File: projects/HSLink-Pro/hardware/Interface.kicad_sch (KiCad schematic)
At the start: 19 parts, among them J1 IDC 2x10p 夹板, J2 USB_C_Receptacle_USB2.0, Q1 AO3401A, Q2 2N7002, Q3 AO3401A, Q4 2N7002, U14 MT9700, U15 ESD0524P, U16 ESD0524P, U17 ESD0524P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

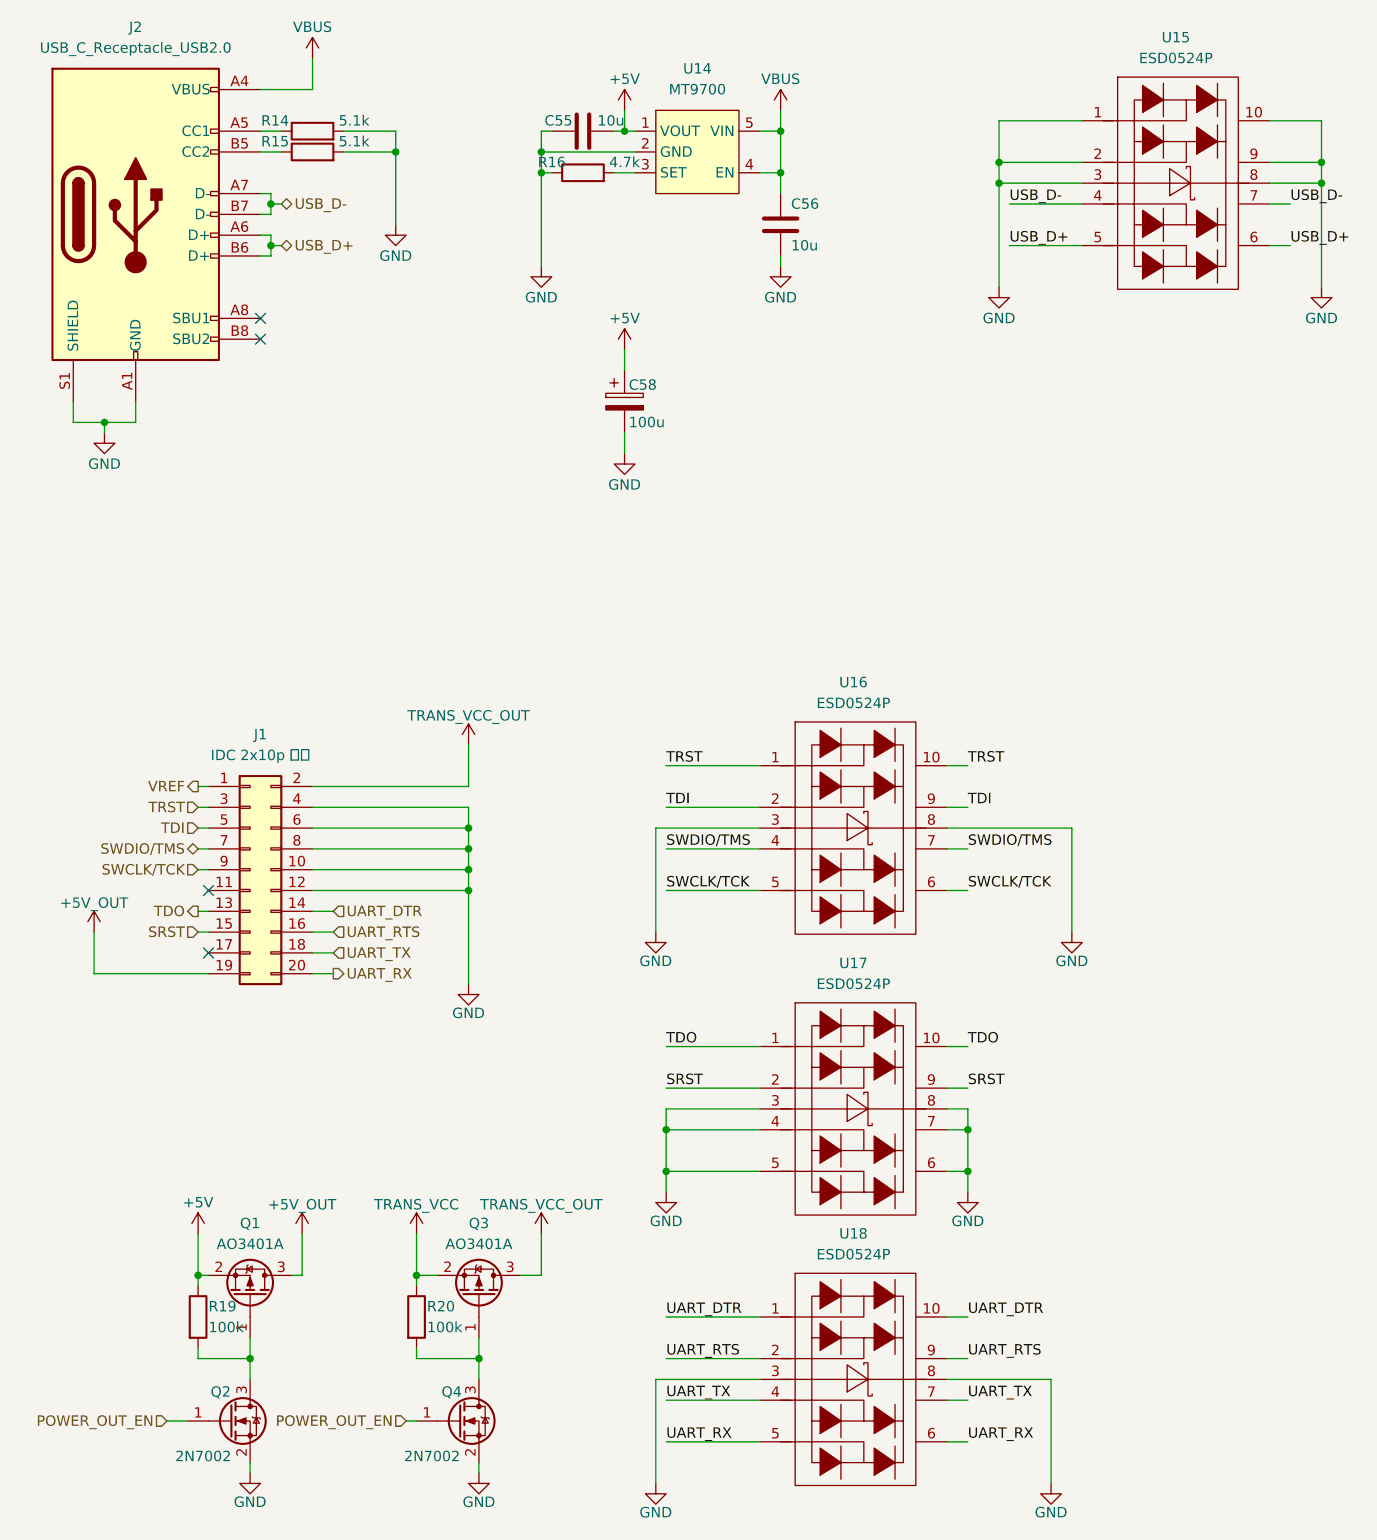
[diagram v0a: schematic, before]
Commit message: HSLink-Pro: 2.3.1 (#29)
* update: 更新电源部分

* update: 更新原理图

* update: 更新PCB

- 修改定位孔位置
- 修改Type-C位置

* update: 添加RTT LOGO

* chore: 添加cJSON库

* feat: 添加与上位机的HID通信接口

* refactor: 重构命令解析部分代码

* fix: 修复描述符错误

* feat: 添加上位机下发设置功能

* feat: 添加数据保存

* fix: 修复可能的一些错误

* fix: 修复写入flash死机问题

* fix: 潜在的内存泄露问题

* chore: 添加tlsf

* chore: 切换cJSON库位置

* feat: 内存管理切换为tlsf

* feat: 添加首次默认设置

* feat: 添加硬件版本号

* feat: 添加获取设置

* chore: 将项目修改为cpp

* feat: 重构为cpp

* fix: 修复release下可能会崩溃的玄学问题

* chore: 删除cJSON库

* fix: 修复RapidJSON库所需内存

* fix: 修复nickname设置问题

* fix: BL工程编译失败

* fix: BL工程里面关闭所有输出

* fix: 修复一些warning

* update: README

* fix: get_setting字段错误

* update: 1.2.0硬件

* style: 统一接口命名

* feat: 添加upgrade命令

* fix: 将硬件版本号放在OTP寄存器中

* fix: 解决初始值问题

* fix: PWM输出极性反了

* fix: 1.2.0硬件修改IO

* release: 2.3.1
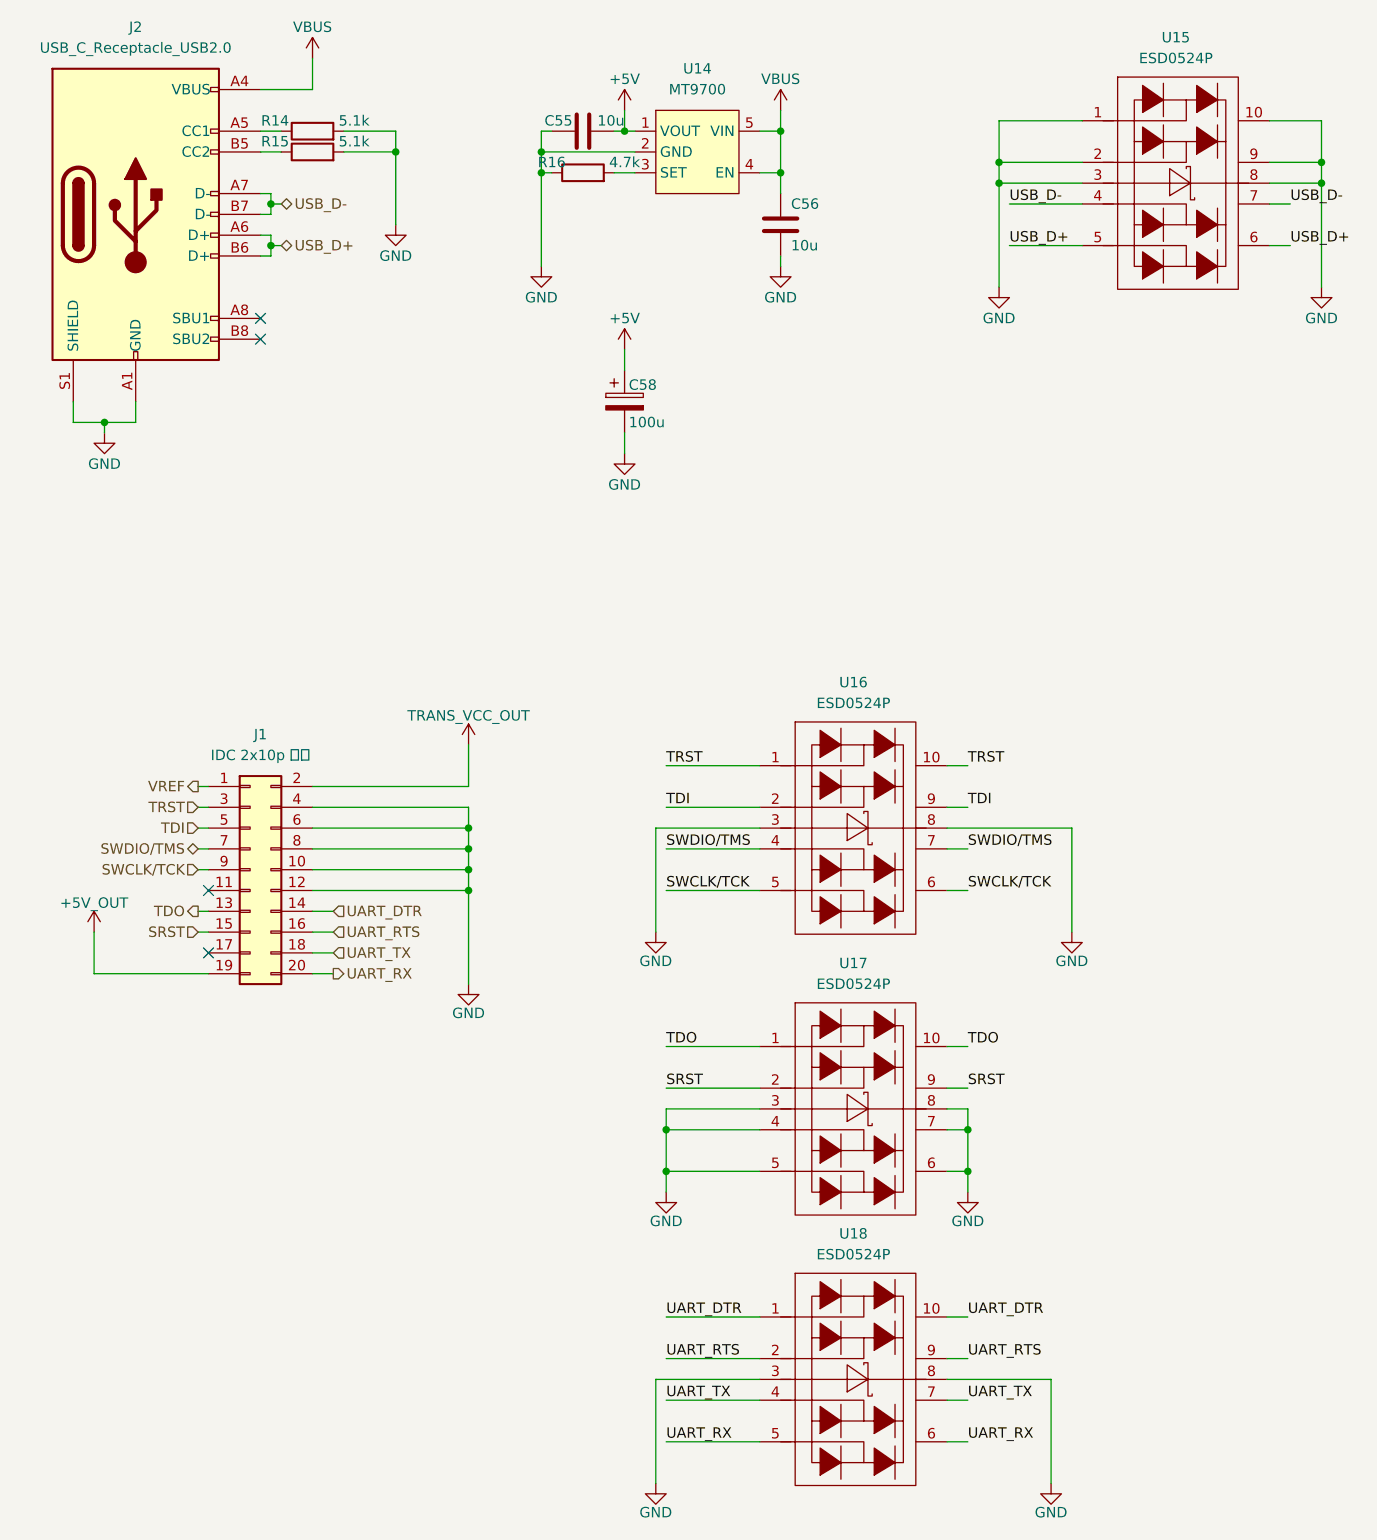
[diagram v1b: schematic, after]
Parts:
- removed Q1, Q3: AO3401A, Package_TO_SOT_SMD:SOT-23, symbol Transistor_FET:AO3401A
- removed Q2, Q4: 2N7002, Package_TO_SOT_SMD:SOT-323_SC-70, symbol Transistor_FET:2N7002
- removed R19, R20: 100k, Resistor_SMD:R_0402_1005Metric, symbol Device:R
